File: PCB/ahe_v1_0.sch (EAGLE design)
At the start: 41 parts, among them CN3 1X4-3.5MM, CN4 1X4-3.5MM, IC1 MS560702BA03-50, IC2 MCP73871-1CCI_ML, IC3 ESP32-S2-WROOM-I_M22S2H3200UH3, J1 USB3075-30-A, Q1 TSM200N03DPQ33_RGG

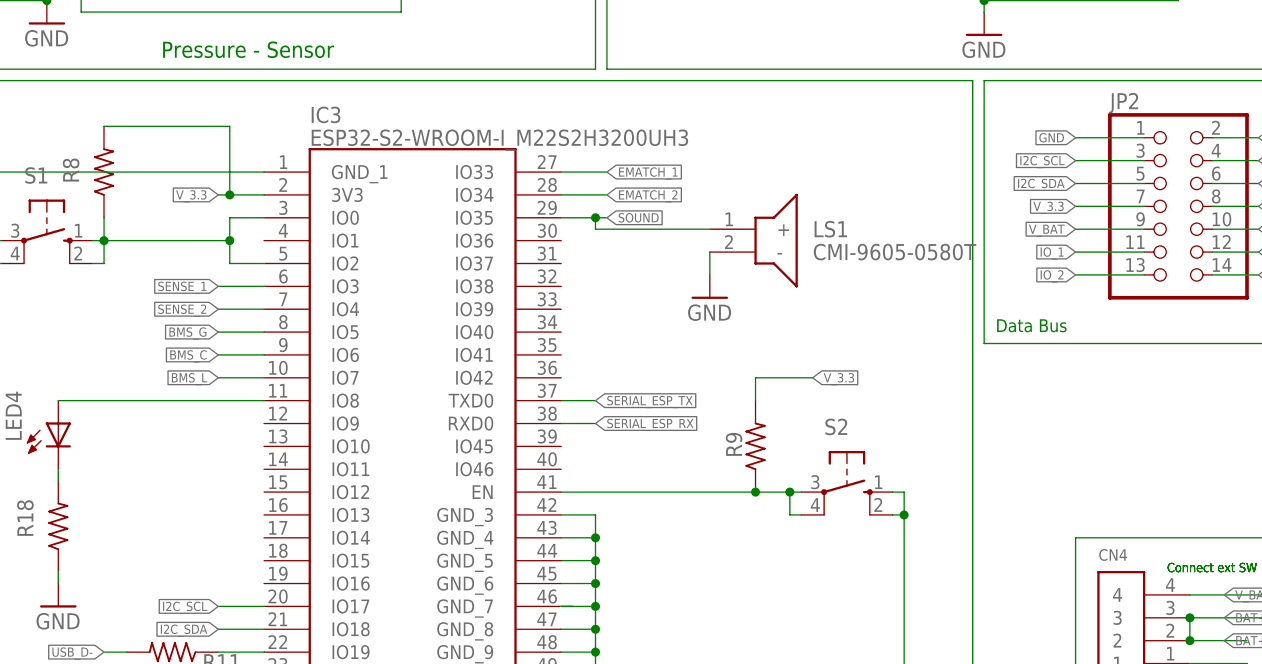
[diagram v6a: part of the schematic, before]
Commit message: fixed schematic bugs in v1_0
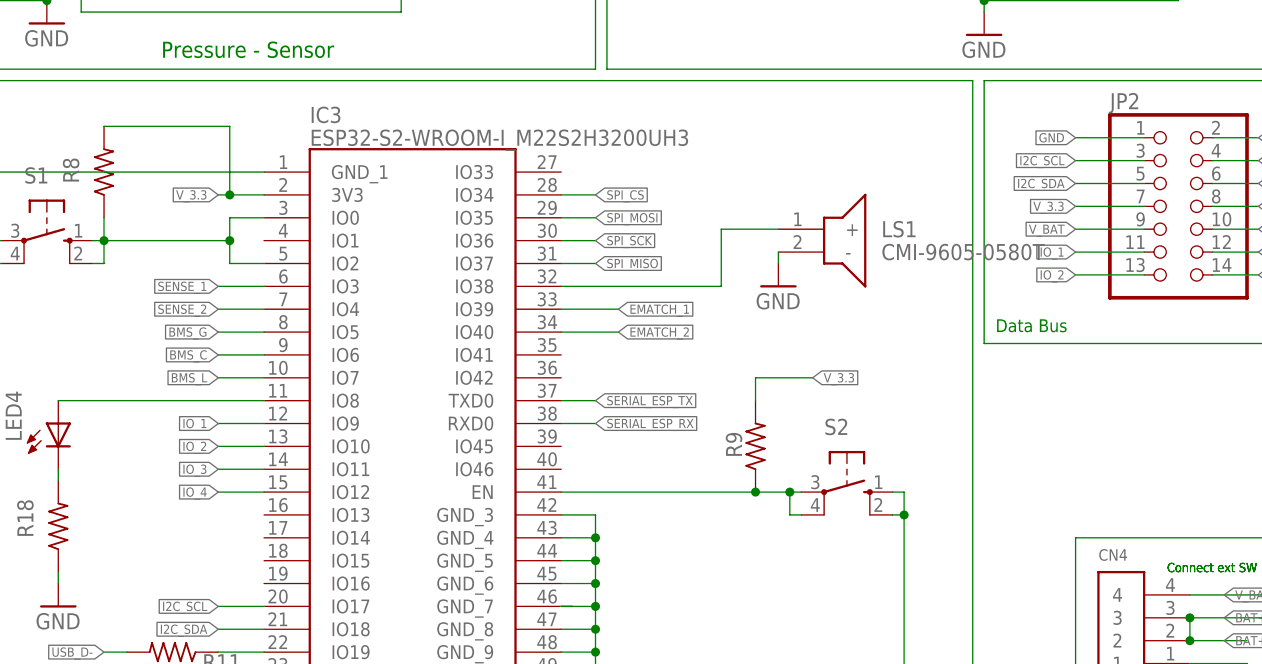
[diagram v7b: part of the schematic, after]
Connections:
- new net SPI_SCK: IC3.IO36
- net EMATCH_1: now also IC3.IO39; no longer IC3.IO33
- net EMATCH_2: now also IC3.IO40; no longer IC3.IO34
- net IO_1: now also IC3.IO9
- net IO_2: now also IC3.IO10
- net IO_3: now also IC3.IO11
- net IO_4: now also IC3.IO12
- net SOUND: now also IC3.IO38; no longer IC3.IO35
- net SPI_CS: now also IC3.IO34
- net SPI_MISO: now also IC3.IO37
- net SPI_MOSI: now also IC3.IO35
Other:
- moved on the sheet: LS1
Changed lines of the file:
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@@
 <attribute name="NAME" x="-117.0686" y="-68.58" size="1.778" layer="95" rot="R90"/>
 </instance>
-<instance part="LS1" gate="G$1" x="-106.68" y="40.64" smashed="yes">
-<attribute name="NAME" x="-95.25" y="40.64" size="1.778" layer="95" align="center-left"/>
-<attribute name="VALUE" x="-95.25" y="38.1" size="1.778" layer="96" align="center-left"/>
-</instance>
-<instance part="GND14" gate="1" x="-106.68" y="33.02" smashed="yes">
-<attribute name="VALUE" x="-109.22" y="30.48" size="1.778" layer="96"/>
+<instance part="LS1" gate="G$1" x="-99.06" y="40.64" smashed="yes">
+<attribute name="NAME" x="-87.63" y="40.64" size="1.778" layer="95" align="center-left"/>
+<attribute name="VALUE" x="-87.63" y="38.1" size="1.778" layer="96" align="center-left"/>
+</instance>
+<instance part="GND14" gate="1" x="-99.06" y="34.29" smashed="yes">
+<attribute name="VALUE" x="-101.6" y="31.75" size="1.778" layer="96"/>
 </instance>
 <instance part="LED1" gate="G$1" x="-135.89" y="162.56" smashed="yes" rot="R90">
@@
 <pinref part="LS1" gate="G$1" pin="-"/>
 <pinref part="GND14" gate="1" pin="GND"/>
-<wire x1="-106.68" y1="38.1" x2="-106.68" y2="35.56" width="0.1524" layer="91"/>
+<wire x1="-99.06" y1="38.1" x2="-99.06" y2="36.83" width="0.1524" layer="91"/>
 </segment>
 <segment>
@@
 <pinref part="JP2" gate="A" pin="2"/>
 </segment>
+<segment>
+<pinref part="IC3" gate="G$1" pin="IO34"/>
+<wire x1="-123.19" y1="44.45" x2="-119.38" y2="44.45" width="0.1524" layer="91"/>
+<label x="-119.38" y="44.45" size="1.016" layer="95" xref="yes"/>
+</segment>
 </net>
 <net name="SPI_MOSI" class="0">
@@
 <pinref part="JP2" gate="A" pin="4"/>
 </segment>
+<segment>
+<pinref part="IC3" gate="G$1" pin="IO35"/>
+<wire x1="-123.19" y1="41.91" x2="-119.38" y2="41.91" width="0.1524" layer="91"/>
+<label x="-119.38" y="41.91" size="1.016" layer="95" xref="yes"/>
+</segment>
 </net>
 <net name="SPI_MISO" class="0">
@@
 <pinref part="JP2" gate="A" pin="6"/>
 </segment>
+<segment>
+<pinref part="IC3" gate="G$1" pin="IO37"/>
+<wire x1="-123.19" y1="36.83" x2="-119.38" y2="36.83" width="0.1524" layer="91"/>
+<label x="-119.38" y="36.83" size="1.016" layer="95" xref="yes"/>
+</segment>
 </net>
 <net name="SPI_SCLK" class="0">
@@
 <label x="-66.04" y="38.1" size="1.016" layer="95" rot="R180" xref="yes"/>
 </segment>
+<segment>
+<pinref part="IC3" gate="G$1" pin="IO9"/>
+<wire x1="-156.21" y1="19.05" x2="-161.29" y2="19.05" width="0.1524" layer="91"/>
+<label x="-161.29" y="19.05" size="1.016" layer="95" rot="R180" xref="yes"/>
+</segment>
 </net>
 <net name="IO_2" class="0">
@@
 <label x="-66.04" y="35.56" size="1.016" layer="95" rot="R180" xref="yes"/>
 </segment>
+<segment>
+<pinref part="IC3" gate="G$1" pin="IO10"/>
+<wire x1="-156.21" y1="16.51" x2="-161.29" y2="16.51" width="0.1524" layer="91"/>
+<label x="-161.29" y="16.51" size="1.016" layer="95" rot="R180" xref="yes"/>
+</segment>
 </net>
 <net name="IO_3" class="0">
@@
 <label x="-45.72" y="38.1" size="1.016" layer="95" xref="yes"/>
 </segment>
+<segment>
+<pinref part="IC3" gate="G$1" pin="IO11"/>
+<wire x1="-156.21" y1="13.97" x2="-161.29" y2="13.97" width="0.1524" layer="91"/>
+<label x="-161.29" y="13.97" size="1.016" layer="95" rot="R180" xref="yes"/>
+</segment>
 </net>
 <net name="IO_4" class="0">
@@
 <wire x1="-50.8" y1="35.56" x2="-45.72" y2="35.56" width="0.1524" layer="91"/>
 <label x="-45.72" y="35.56" size="1.016" layer="95" xref="yes"/>
+</segment>
+<segment>
+<pinref part="IC3" gate="G$1" pin="IO12"/>
+<wire x1="-156.21" y1="11.43" x2="-161.29" y2="11.43" width="0.1524" layer="91"/>
+<label x="-161.29" y="11.43" size="1.016" layer="95" rot="R180" xref="yes"/>
 </segment>
 </net>
@@
 <net name="EMATCH_1" class="0">
 <segment>
-<pinref part="IC3" gate="G$1" pin="IO33"/>
-<wire x1="-123.19" y1="46.99" x2="-118.11" y2="46.99" width="0.1524" layer="91"/>
-<label x="-118.11" y="46.99" size="1.016" layer="95" xref="yes"/>
-</segment>
-<segment>
 <pinref part="Q1" gate="G$1" pin="GATE1"/>
 <wire x1="-173.99" y1="-43.18" x2="-179.07" y2="-43.18" width="0.1524" layer="91"/>
 <label x="-179.07" y="-43.18" size="1.778" layer="95" rot="R180" xref="yes"/>
 </segment>
+<segment>
+<pinref part="IC3" gate="G$1" pin="IO39"/>
+<wire x1="-123.19" y1="31.75" x2="-116.84" y2="31.75" width="0.1524" layer="91"/>
+<label x="-116.84" y="31.75" size="1.016" layer="95" xref="yes"/>
+</segment>
 </net>
 <net name="EMATCH_2" class="0">
-<segment>
-<pinref part="IC3" gate="G$1" pin="IO34"/>
-<wire x1="-123.19" y1="44.45" x2="-118.11" y2="44.45" width="0.1524" layer="91"/>
-<label x="-118.11" y="44.45" size="1.016" layer="95" xref="yes"/>
-</segment>
 <segment>
 <pinref part="Q1" gate="G$1" pin="GATE2"/>
@@
 <label x="-179.07" y="-48.26" size="1.778" layer="95" rot="R180" xref="yes"/>
 </segment>
+<segment>
+<pinref part="IC3" gate="G$1" pin="IO40"/>
+<wire x1="-123.19" y1="29.21" x2="-116.84" y2="29.21" width="0.1524" layer="91"/>
+<label x="-116.84" y="29.21" size="1.016" layer="95" xref="yes"/>
+</segment>
 </net>
 <net name="SOUND" class="0">
 <segment>
-<pinref part="IC3" gate="G$1" pin="IO35"/>
-<wire x1="-123.19" y1="41.91" x2="-119.38" y2="41.91" width="0.1524" layer="91"/>
-<label x="-118.11" y="41.91" size="1.016" layer="95" xref="yes"/>
 <pinref part="LS1" gate="G$1" pin="+"/>
-<wire x1="-119.38" y1="41.91" x2="-118.11" y2="41.91" width="0.1524" layer="91"/>
-<wire x1="-119.38" y1="41.91" x2="-119.38" y2="40.64" width="0.1524" layer="91"/>
-<wire x1="-119.38" y1="40.64" x2="-106.68" y2="40.64" width="0.1524" layer="91"/>
-<junction x="-119.38" y="41.91"/>
+<pinref part="IC3" gate="G$1" pin="IO38"/>
+<wire x1="-105.41" y1="40.64" x2="-99.06" y2="40.64" width="0.1524" layer="91"/>
+<wire x1="-105.41" y1="40.64" x2="-105.41" y2="34.29" width="0.1524" layer="91"/>
+<wire x1="-105.41" y1="34.29" x2="-123.19" y2="34.29" width="0.1524" layer="91"/>
 </segment>
 </net>
@@
 </segment>
 </net>
+<net name="SPI_SCK" class="0">
+<segment>
+<pinref part="IC3" gate="G$1" pin="IO36"/>
+<wire x1="-123.19" y1="39.37" x2="-119.38" y2="39.37" width="0.1524" layer="91"/>
+<label x="-119.38" y="39.37" size="1.016" layer="95" xref="yes"/>
+</segment>
+</net>

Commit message: Final schematic and board for ESP32-S2
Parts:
- removed JP3: (no value), pinhead:PINHD-1X4/90
- removed RT1: 103KT1005T-1P, 103KT1005T-1P:103KT1005T-1P
- added JP4: (no value), pinhead:PINHD-1X2
- added JP5: (no value), pinhead:PINHD-1X4
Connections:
- removed net N$9: IC3.EN, R9.1, S2.P, S2.P1
- new net N$24: IC3.EN, R9.1, S2.S, S2.S1
- net GND: now also JP4.1, JP5.1, S2.P, S2.P1; no longer JP3.1, RT1.1, S2.S, S2.S1
- net N$3: now also JP4.2; no longer RT1.2
- net SERIAL_ESP_RX: now also JP5.2; no longer JP3.2
- net SERIAL_ESP_TX: now also JP5.3; no longer JP3.3
- net VCC: now also JP5.4; no longer JP3.4
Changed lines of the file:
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@@
 <setting verticaltext="up"/>
 </settings>
-<grid distance="0.05" unitdist="inch" unit="inch" style="lines" multiple="1" display="yes" altdistance="0.01" altunitdist="inch" altunit="inch"/>
+<grid distance="0.05" unitdist="inch" unit="inch" style="lines" multiple="1" display="no" altdistance="0.01" altunitdist="inch" altunit="inch"/>
 <layers>
 <layer number="1" name="Top" color="4" fill="1" visible="no" active="no"/>
@@
 <clearance class="1" value="0.1524"/>
 </class>
+<class number="2" name="V_bat" width="0.3048" drill="0">
+<clearance class="2" value="0.1524"/>
+</class>
 </classes>
 <parts>
@@
 <part name="GND5" library="supply1" library_urn="urn:adsk.eagle:library:371" deviceset="GND" device=""/>
 <part name="P+3" library="supply1" library_urn="urn:adsk.eagle:library:371" deviceset="VCC" device=""/>
-<part name="RT1" library="103KT1005T-1P" deviceset="103KT1005T-1P" device=""/>
 <part name="GND6" library="supply1" library_urn="urn:adsk.eagle:library:371" deviceset="GND" device=""/>
 <part name="PS1" library="BU33SD5WG-TR" deviceset="BU33SD5WG-TR" device=""/>
@@
 <part name="GND8" library="supply1" library_urn="urn:adsk.eagle:library:371" deviceset="GND" device=""/>
 <part name="JP2" library="pinhead" library_urn="urn:adsk.eagle:library:325" deviceset="PINHD-2X7" device="" package3d_urn="urn:adsk.eagle:package:22478/2"/>
-<part name="JP3" library="pinhead" library_urn="urn:adsk.eagle:library:325" deviceset="PINHD-1X4" device="/90" package3d_urn="urn:adsk.eagle:package:22404/2"/>
 <part name="R10" library="rcl" library_urn="urn:adsk.eagle:library:334" deviceset="R-US_" device="R0805" package3d_urn="urn:adsk.eagle:package:23553/2" value="33"/>
 <part name="R11" library="rcl" library_urn="urn:adsk.eagle:library:334" deviceset="R-US_" device="R0805" package3d_urn="urn:adsk.eagle:package:23553/2" value="33"/>
@@
 <part name="CN4" library="adafruit" deviceset="1X4" device="-3.5MM"/>
 <part name="JP1" library="pinhead" library_urn="urn:adsk.eagle:library:325" deviceset="PINHD-1X2" device="" package3d_urn="urn:adsk.eagle:package:22435/2"/>
+<part name="JP4" library="pinhead" library_urn="urn:adsk.eagle:library:325" deviceset="PINHD-1X2" device="" package3d_urn="urn:adsk.eagle:package:22435/2"/>
+<part name="JP5" library="pinhead" library_urn="urn:adsk.eagle:library:325" deviceset="PINHD-1X4" device="" package3d_urn="urn:adsk.eagle:package:22407/2"/>
 </parts>
 <sheets>
@@
 <attribute name="VALUE" x="-85.09" y="149.86" size="1.778" layer="96" rot="R90"/>
 </instance>
-<instance part="RT1" gate="G$1" x="-96.52" y="106.68" smashed="yes">
-<attribute name="NAME" x="-93.98" y="113.03" size="1.778" layer="95" align="center-left"/>
-<attribute name="VALUE" x="-93.98" y="110.49" size="1.778" layer="96" align="center-left"/>
-</instance>
 <instance part="GND6" gate="1" x="-96.52" y="101.6" smashed="yes">
 <attribute name="VALUE" x="-99.06" y="99.06" size="1.778" layer="96"/>
@@
 <attribute name="NAME" x="-103.0986" y="15.24" size="1.778" layer="95" rot="R90"/>
 </instance>
-<instance part="S2" gate="1" x="-91.44" y="11.43" smashed="yes" rot="R270">
-<attribute name="NAME" x="-93.98" y="17.78" size="1.778" layer="95"/>
-<attribute name="VALUE" x="-88.265" y="15.24" size="1.778" layer="96"/>
+<instance part="S2" gate="1" x="-91.44" y="11.43" smashed="yes" rot="MR270">
+<attribute name="NAME" x="-88.9" y="17.78" size="1.778" layer="95" rot="MR0"/>
+<attribute name="VALUE" x="-94.615" y="15.24" size="1.778" layer="96" rot="MR0"/>
 </instance>
 <instance part="GND8" gate="1" x="-160.02" y="-22.86" smashed="yes">
@@
 <attribute name="VALUE" x="-62.23" y="30.48" size="1.778" layer="96"/>
 </instance>
-<instance part="JP3" gate="A" x="-123.19" y="129.54" smashed="yes">
-<attribute name="NAME" x="-129.54" y="137.795" size="1.778" layer="95"/>
-<attribute name="VALUE" x="-129.54" y="121.92" size="1.778" layer="96"/>
-</instance>
 <instance part="R10" gate="G$1" x="-166.37" y="-8.89" smashed="yes" rot="R180">
 <attribute name="NAME" x="-160.02" y="-10.3886" size="1.778" layer="95" rot="R180"/>
@@
 <attribute name="NAME" x="-39.37" y="3.175" size="1.778" layer="95"/>
 <attribute name="VALUE" x="-39.37" y="-7.62" size="1.778" layer="96"/>
+</instance>
+<instance part="JP4" gate="G$1" x="-88.9" y="111.76" smashed="yes" rot="R90">
+<attribute name="NAME" x="-94.615" y="105.41" size="1.778" layer="95" rot="R90"/>
+<attribute name="VALUE" x="-83.82" y="105.41" size="1.778" layer="96" rot="R90"/>
+</instance>
+<instance part="JP5" gate="A" x="-123.19" y="129.54" smashed="yes">
+<attribute name="NAME" x="-129.54" y="137.795" size="1.778" layer="95"/>
+<attribute name="VALUE" x="-129.54" y="121.92" size="1.778" layer="96"/>
 </instance>
 </instances>
@@
 </segment>
 <segment>
-<pinref part="JP3" gate="A" pin="4"/>
 <wire x1="-125.73" y1="127" x2="-133.35" y2="127" width="0.1524" layer="91"/>
 <label x="-133.35" y="127" size="1.016" layer="95" rot="R180" xref="yes"/>
+<pinref part="JP5" gate="A" pin="4"/>
 </segment>
 <segment>
@@
 </segment>
 </net>
-<net name="GND" class="0">
+<net name="GND" class="2">
 <segment>
 <pinref part="J1" gate="G$1" pin="5"/>
@@
 </segment>
 <segment>
-<pinref part="RT1" gate="G$1" pin="1"/>
 <pinref part="GND6" gate="1" pin="GND"/>
-<wire x1="-96.52" y1="106.68" x2="-96.52" y2="104.14" width="0.1524" layer="91"/>
+<pinref part="JP4" gate="G$1" pin="1"/>
+<wire x1="-91.44" y1="109.22" x2="-91.44" y2="104.14" width="0.1524" layer="91"/>
+<wire x1="-91.44" y1="104.14" x2="-96.52" y2="104.14" width="0.1524" layer="91"/>
 </segment>
 <segment>
@@
 <wire x1="-119.38" y1="-17.78" x2="-119.38" y2="-13.97" width="0.1524" layer="91"/>
 <wire x1="-119.38" y1="-13.97" x2="-85.09" y2="-13.97" width="0.1524" layer="91"/>
-<pinref part="S2" gate="1" pin="S"/>
+<wire x1="-85.09" y1="-13.97" x2="-85.09" y2="8.89" width="0.1524" layer="91"/>
+<pinref part="S2" gate="1" pin="P"/>
+<wire x1="-85.09" y1="8.89" x2="-85.09" y2="11.43" width="0.1524" layer="91"/>
 <wire x1="-86.36" y1="11.43" x2="-85.09" y2="11.43" width="0.1524" layer="91"/>
-<pinref part="S2" gate="1" pin="S1"/>
-<wire x1="-85.09" y1="11.43" x2="-85.09" y2="8.89" width="0.1524" layer="91"/>
-<wire x1="-85.09" y1="8.89" x2="-86.36" y2="8.89" width="0.1524" layer="91"/>
-<wire x1="-85.09" y1="-13.97" x2="-85.09" y2="8.89" width="0.1524" layer="91"/>
+<pinref part="S2" gate="1" pin="P1"/>
+<wire x1="-86.36" y1="8.89" x2="-85.09" y2="8.89" width="0.1524" layer="91"/>
 <junction x="-85.09" y="8.89"/>
 </segment>
@@
 </segment>
 <segment>
-<pinref part="JP3" gate="A" pin="1"/>
 <wire x1="-125.73" y1="134.62" x2="-133.35" y2="134.62" width="0.1524" layer="91"/>
 <label x="-133.35" y="134.62" size="1.016" layer="95" rot="R180" xref="yes"/>
+<pinref part="JP5" gate="A" pin="1"/>
 </segment>
 <segment>
@@
 <net name="N$3" class="0">
 <segment>
-<pinref part="RT1" gate="G$1" pin="2"/>
 <pinref part="IC2" gate="G$1" pin="THERM"/>
-<wire x1="-78.74" y1="106.68" x2="-72.39" y2="106.68" width="0.1524" layer="91"/>
+<pinref part="JP4" gate="G$1" pin="2"/>
+<wire x1="-88.9" y1="109.22" x2="-88.9" y2="106.68" width="0.1524" layer="91"/>
+<wire x1="-88.9" y1="106.68" x2="-72.39" y2="106.68" width="0.1524" layer="91"/>
 </segment>
 </net>
@@
 </segment>
 <segment>
-<pinref part="JP3" gate="A" pin="3"/>
 <wire x1="-125.73" y1="129.54" x2="-133.35" y2="129.54" width="0.1524" layer="91"/>
 <label x="-133.35" y="129.54" size="1.016" layer="95" rot="R180" xref="yes"/>
+<pinref part="JP5" gate="A" pin="3"/>
 </segment>
 </net>
@@
 </segment>
 <segment>
-<pinref part="JP3" gate="A" pin="2"/>
 <wire x1="-125.73" y1="132.08" x2="-133.35" y2="132.08" width="0.1524" layer="91"/>
 <label x="-133.35" y="132.08" size="1.016" layer="95" rot="R180" xref="yes"/>
+<pinref part="JP5" gate="A" pin="2"/>
 </segment>
 </net>
@@
 </segment>
 </net>
-<net name="N$9" class="0">
-<segment>
-<pinref part="IC3" gate="G$1" pin="EN"/>
-<wire x1="-123.19" y1="11.43" x2="-101.6" y2="11.43" width="0.1524" layer="91"/>
-<pinref part="R9" gate="G$1" pin="1"/>
-<pinref part="S2" gate="1" pin="P"/>
-<wire x1="-101.6" y1="11.43" x2="-97.79" y2="11.43" width="0.1524" layer="91"/>
-<junction x="-101.6" y="11.43"/>
-<pinref part="S2" gate="1" pin="P1"/>
-<wire x1="-97.79" y1="11.43" x2="-96.52" y2="11.43" width="0.1524" layer="91"/>
-<wire x1="-97.79" y1="11.43" x2="-97.79" y2="8.89" width="0.1524" layer="91"/>
-<wire x1="-97.79" y1="8.89" x2="-96.52" y2="8.89" width="0.1524" layer="91"/>
-<junction x="-97.79" y="11.43"/>
-</segment>
-</net>
 <net name="SPI_CS" class="0">
 <segment>
@@
 </segment>
 </net>
-<net name="EMATCH_2-" class="1">
+<net name="EMATCH_2-" class="2">
 <segment>
 <pinref part="Q1" gate="G$1" pin="DRAIN2_2"/>
@@
 </segment>
 </net>
+<net name="N$24" class="0">
+<segment>
+<pinref part="S2" gate="1" pin="S1"/>
+<pinref part="IC3" gate="G$1" pin="EN"/>
+<wire x1="-123.19" y1="11.43" x2="-101.6" y2="11.43" width="0.1524" layer="91"/>
+<pinref part="R9" gate="G$1" pin="1"/>
+<wire x1="-101.6" y1="11.43" x2="-97.79" y2="11.43" width="0.1524" layer="91"/>
+<junction x="-101.6" y="11.43"/>
+<wire x1="-97.79" y1="11.43" x2="-97.79" y2="8.89" width="0.1524" layer="91"/>
+<pinref part="S2" gate="1" pin="S"/>
+<wire x1="-96.52" y1="11.43" x2="-97.79" y2="11.43" width="0.1524" layer="91"/>
+<junction x="-97.79" y="11.43"/>
+<wire x1="-96.52" y1="8.89" x2="-97.79" y2="8.89" width="0.1524" layer="91"/>
+</segment>
+</net>
